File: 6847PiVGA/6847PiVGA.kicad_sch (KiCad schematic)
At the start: 38 parts, among them J1 DB15_Female_HighDensity, U1 MC6847, U2 AD724JRZ, U3 Pico, U4 AD813, Y1 4.433620MHz

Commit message: refine hardware layout
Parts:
- J1: footprint Resistor_SMD:R_0603_1608Metric -> Connector_Dsub:DSUB-15-HD_Female_Horizontal_P2.29x1.98mm_EdgePinOffset3.03mm_Housed_MountingHolesOffset4.94mm
- U3: footprint RPi_Pico:RPi_Pico_SMD_TH -> Package_DIP:DIP-42_W15.24mm
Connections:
- net at R12.1, R7.1, R8.1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: now also C1.2, J1.3; no longer C3.2, J1.1
- net at R1.1, R10.1, R2.1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: now also C3.2, J1.1; no longer C1.2, J1.3
- no-connect marks 19 -> 31

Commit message: board refresh
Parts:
- C1, C10, C2, C3, C4, C5, C6, C7, C8, C9: footprint Capacitor_SMD:C_0603_1608Metric -> Capacitor_SMD:C_0805_2012Metric
- R1, R10, R11, R12, R13, R14, R15, R16, R17, R18, R19, R20, R21, R22, R5, R8: footprint Resistor_SMD:R_0603_1608Metric -> Resistor_SMD:R_0805_2012Metric
- R2: value 1K -> 2K; footprint Resistor_SMD:R_0603_1608Metric -> Resistor_SMD:R_0805_2012Metric
- R3, R6, R9: value 2K -> 499R; footprint Resistor_SMD:R_0603_1608Metric -> Resistor_SMD:R_0805_2012Metric
- R4, R7: value 499R -> 2K; footprint Resistor_SMD:R_0603_1608Metric -> Resistor_SMD:R_0805_2012Metric
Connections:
- net +5V: now also U3.39 (VSYS); no longer U3.40 (VBUS)
- net GND: now also J1.10, J1.5, J1.7, U3.18 (GND), U3.23 (GND), U3.28 (GND), U3.3 (GND), U3.33 (AGND), U3.8 (GND)
- net Vsync: now reaches U1.12 (~{MS}), U1.37 (~{FS}), U2.15 (VSYNC), U3.17 (GPIO13)
- net Vsync: now also J1.14; no longer J1.13
- net DD6: now reaches U1.2 (DD6), U1.32 (INV), U3.9 (GPIO6)
- net Atiming: now reaches U1.22 (DA0), U3.20 (GPIO15)
- net GM2: now reaches U1.27 (GM2), U3.14 (GPIO10)
- net GM1: now reaches U1.29 (GM1), U3.12 (GPIO9)
- net DD0: now reaches U1.3 (DD0), U3.1 (GPIO0)
- net GM0: now reaches U1.30 (GM0), U1.31 (~{INT}/EXT), U3.11 (GPIO8)
- net CLK: now reaches U1.33 (CLK), U3.16 (GPIO12)
- net DD7: now reaches U1.34 (~{A}/S), U1.40 (DD7), U3.10 (GPIO7)
- net ~{A}/G: now reaches U1.35 (~{A}/G), U3.19 (GPIO14)
- net Hsync: now reaches U1.38 (~{HS}), U2.16 (HSYNC), U3.21 (GPIO16)
- net Hsync: now also J1.13; no longer J1.14
- net CSS: now reaches U1.39 (CSS), U3.15 (GPIO11)
- net DD1: now reaches U1.4 (DD1), U3.2 (GPIO1)
- net DD2: now reaches U1.5 (DD2), U3.4 (GPIO2)
- net DD3: now reaches U1.6 (DD3), U3.5 (GPIO3)
- net DD4: now reaches U1.7 (DD4), U3.6 (GPIO4)
- net DD5: now reaches U1.8 (DD5), U3.7 (GPIO5)
- net Gvga: now reaches C2.2, J1.2, R11.1, R4.1, R5.1, R6.1, U4.12 (+)
- net at R6.2: now also U3.29 (GPIO22); no longer U3.26 (GPIO20)
- net Bvga: now reaches C1.2, J1.3, R12.1, R7.1, R8.1, R9.1, U4.10 (+)
- net at R7.2: now also U3.22 (GPIO17); no longer U3.25 (GPIO19)
- net Composite: now reaches C9.1, U2.10 (COMP)
- net Rin: now reaches C3.1, U2.6 (RIN)
- net Gin: now reaches C2.1, U2.7 (GIN)
- net Bin: now reaches C1.1, U2.8 (BIN)
- net Rvga: now reaches C3.2, J1.1, R1.1, R10.1, R2.1, R3.1, U4.5 (+)
- net at R3.2: now also U3.34 (GPIO28_ADC2); no longer U3.31 (GPIO26_ADC0)
- net at R9.2: now also U3.25 (GPIO19); no longer U3.22 (GPIO17)
- net at R4.2: now also U3.26 (GPIO20); no longer U3.29 (GPIO22)
- net at R1.2: now also U3.31 (GPIO26_ADC0); no longer U3.34 (GPIO28_ADC2)
- no-connect marks 31 -> 28
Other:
- moved on the sheet: C1, C10, C2, C3, C4, C5, C6, C7, C8, C9, J1, R1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

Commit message: add power protection
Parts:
- added C11: 10uF, Capacitor_SMD:C_0805_2012Metric, symbol Device:C
- added D1: 1N5817, Diode_SMD:D_SOD-523, symbol Diode:1N5817
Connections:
- net +5V: now also C11.1, D1.2 (A); no longer U3.39 (VSYS)
- net GND: now also C11.2
- new net: D1.1 (K), U3.39 (VSYS)
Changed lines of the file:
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@@
     (comment 2 "Provides VGA, RGB and Composite video output")
   )
+  (junction (at 142.875 48.895) (diameter 0) (color 0 0 0 0)
+  )
   (junction (at 42.164 23.749) (diameter 0) (color 0 0 0 0)
   )
@@
   )
   (junction (at 262.763 24.511) (diameter 0) (color 0 0 0 0)
+  )
+  (junction (at 142.875 56.515) (diameter 0) (color 0 0 0 0)
   )
   (junction (at 237.363 49.911) (diameter 0) (color 0 0 0 0)
@@
     (stroke (width 0) (type default) (color 0 0 0 0))
   )
+  (wire (pts (xy 136.525 48.895) (xy 142.875 48.895))
+    (stroke (width 0) (type default) (color 0 0 0 0))
+  )
   (wire (pts (xy 127 74.295) (xy 125.73 74.295))
     (stroke (width 0) (type default) (color 0 0 0 0))
@@
     (stroke (width 0) (type default) (color 0 0 0 0))
   )
+  (wire (pts (xy 142.875 56.515) (xy 125.73 56.515))
+    (stroke (width 0) (type default) (color 0 0 0 0))
+  )
   (wire (pts (xy 40.005 145.923) (xy 28.448 145.923))
     (stroke (width 0) (type default) (color 0 0 0 0))
@@
     (stroke (width 0) (type default) (color 0 0 0 0))
   )
+  (wire (pts (xy 136.525 53.975) (xy 136.525 48.895))
+    (stroke (width 0) (type default) (color 0 0 0 0))
+  )
   (wire (pts (xy 29.718 138.303) (xy 31.115 138.303))
     (stroke (width 0) (type default) (color 0 0 0 0))
@@
   )
   (wire (pts (xy 42.164 23.749) (xy 42.164 25.527))
+    (stroke (width 0) (type default) (color 0 0 0 0))
+  )
+  (wire (pts (xy 128.905 53.975) (xy 125.73 53.975))
     (stroke (width 0) (type default) (color 0 0 0 0))
   )
@@
       (effects (font (size 1.27 1.27)) hide)
     )
+    (pin "1")
+    (pin "5")
+    (pin "6")
+    (pin "7")
+    (pin "12")
+    (pin "13")
+    (pin "14")
+    (pin "2")
     (pin "10")
     (pin "3")
     (pin "8")
     (pin "9")
+    (pin "11")
+    (pin "4")
   )
   (symbol (lib_id "power:GND") (at 90.17 94.615 270) (unit 1)
@@
     (pin "1")
   )
+  (symbol (lib_id "power:+5V") (at 142.875 48.895 270) (unit 1)
+    (in_bom yes) (on_board yes) (fields_autoplaced)
+    (property "Reference" "#PWR02" (id 0) (at 139.065 48.895 0)
+      (effects (font (size 1.27 1.27)) hide)
+    )
+    (property "Value" "+5V" (id 1) (at 146.685 48.8949 90)
+      (effects (font (size 1.27 1.27)) (justify left))
+    )
+    (property "Footprint" "" (id 2) (at 142.875 48.895 0)
+      (effects (font (size 1.27 1.27)) hide)
+    )
+    (property "Datasheet" "" (id 3) (at 142.875 48.895 0)
+      (effects (font (size 1.27 1.27)) hide)
+    )
+    (pin "1")
+  )
   (symbol (lib_id "power:GND") (at 125.73 69.215 90) (unit 1)
     (in_bom yes) (on_board yes) (fields_autoplaced)
@@
     )
     (pin "1")
+  )
+  (symbol (lib_id "Diode:1N5817") (at 132.715 53.975 0) (unit 1)
+    (in_bom yes) (on_board yes) (fields_autoplaced)
+    (property "Reference" "D1" (id 0) (at 132.3975 47.625 0))
+    (property "Value" "1N5817" (id 1) (at 132.3975 50.165 0))
+    (property "Footprint" "Diode_SMD:D_SOD-523" (id 2) (at 132.715 58.42 0)
+      (effects (font (size 1.27 1.27)) hide)
+    )
+    (property "Datasheet" "http://www.vishay.com/docs/88525/1n5817.pdf" (id 3) (at 132.715 53.975 0)
+      (effects (font (size 1.27 1.27)) hide)
+    )
+    (pin "1")
+    (pin "2")
   )
   (symbol (lib_id "Device:R") (at 130.81 84.455 270) (unit 1)
@@
       (effects (font (size 1.27 1.27)) hide)
     )
+    (pin "1")
+    (pin "5")
+    (pin "6")
+    (pin "7")
+    (pin "12")
+    (pin "13")
+    (pin "14")
+    (pin "2")
+    (pin "10")
+    (pin "3")
+    (pin "8")
+    (pin "9")
     (pin "11")
     (pin "4")
@@
     (pin "2")
   )
-  (symbol (lib_id "power:GND") (at 125.73 56.515 90) (unit 1)
-    (in_bom yes) (on_board yes) (fields_autoplaced)
-    (property "Reference" "#PWR0115" (id 0) (at 132.08 56.515 0)
-      (effects (font (size 1.27 1.27)) hide)
-    )
-    (property "Value" "GND" (id 1) (at 129.54 56.5149 90)
-      (effects (font (size 1.27 1.27)) (justify right) hide)
-    )
-    (property "Footprint" "" (id 2) (at 125.73 56.515 0)
-      (effects (font (size 1.27 1.27)) hide)
-    )
-    (property "Datasheet" "" (id 3) (at 125.73 56.515 0)
+  (symbol (lib_id "power:GND") (at 142.875 56.515 90) (unit 1)
+    (in_bom yes) (on_board yes) (fields_autoplaced)
+    (property "Reference" "#PWR0115" (id 0) (at 149.225 56.515 0)
+      (effects (font (size 1.27 1.27)) hide)
+    )
+    (property "Value" "GND" (id 1) (at 146.685 56.5149 90)
+      (effects (font (size 1.27 1.27)) (justify right) hide)
+    )
+    (property "Footprint" "" (id 2) (at 142.875 56.515 0)
+      (effects (font (size 1.27 1.27)) hide)
+    )
+    (property "Datasheet" "" (id 3) (at 142.875 56.515 0)
       (effects (font (size 1.27 1.27)) hide)
     )
@@
     (pin "1")
   )
+  (symbol (lib_id "Device:C") (at 142.875 52.705 0) (unit 1)
+    (in_bom yes) (on_board yes) (fields_autoplaced)
+    (property "Reference" "C11" (id 0) (at 146.685 51.4349 0)
+      (effects (font (size 1.27 1.27)) (justify left))
+    )
+    (property "Value" "10uF" (id 1) (at 146.685 53.9749 0)
+      (effects (font (size 1.27 1.27)) (justify left))
+    )
+    (property "Footprint" "Capacitor_SMD:C_0805_2012Metric" (id 2) (at 143.8402 56.515 0)
+      (effects (font (size 1.27 1.27)) hide)
+    )
+    (property "Datasheet" "~" (id 3) (at 142.875 52.705 0)
+      (effects (font (size 1.27 1.27)) hide)
+    )
+    (pin "1")
+    (pin "2")
+  )
   (symbol (lib_id "Device:R") (at 256.413 49.911 90) (unit 1)
     (in_bom yes) (on_board yes) (fields_autoplaced)
@@
       (effects (font (size 1.27 1.27)) hide)
     )
+    (pin "1")
+    (pin "5")
+    (pin "6")
+    (pin "7")
     (pin "12")
     (pin "13")
     (pin "14")
     (pin "2")
-  )
-  (symbol (lib_id "power:+5V") (at 125.73 53.975 270) (unit 1)
-    (in_bom yes) (on_board yes) (fields_autoplaced)
-    (property "Reference" "#PWR02" (id 0) (at 121.92 53.975 0)
-      (effects (font (size 1.27 1.27)) hide)
-    )
-    (property "Value" "+5V" (id 1) (at 129.54 53.9749 90)
-      (effects (font (size 1.27 1.27)) (justify left))
-    )
-    (property "Footprint" "" (id 2) (at 125.73 53.975 0)
-      (effects (font (size 1.27 1.27)) hide)
-    )
-    (property "Datasheet" "" (id 3) (at 125.73 53.975 0)
-      (effects (font (size 1.27 1.27)) hide)
-    )
-    (pin "1")
+    (pin "10")
+    (pin "3")
+    (pin "8")
+    (pin "9")
+    (pin "11")
+    (pin "4")
   )
   (symbol (lib_id "power:GND") (at 210.185 85.725 0) (unit 1)
@@
     (pin "6")
     (pin "7")
+    (pin "12")
+    (pin "13")
+    (pin "14")
+    (pin "2")
+    (pin "10")
+    (pin "3")
+    (pin "8")
+    (pin "9")
+    (pin "11")
+    (pin "4")
   )
   (symbol (lib_id "Device:C") (at 208.28 99.695 0) (unit 1)
@@
       (reference "#PWR01") (unit 1) (value "GND") (footprint "")
     )
-    (path "/7a749901-be0b-4432-aaf8-b59971568121"
+    (path "/26cb9b96-c0cb-40c8-90fa-6343f70293fe"
       (reference "#PWR02") (unit 1) (value "+5V") (footprint "")
     )
@@
       (reference "C10") (unit 1) (value "0.1uF") (footprint "Capacitor_SMD:C_0805_2012Metric")
     )
+    (path "/70beb333-84c4-4efc-9f6a-99dcba956560"
+      (reference "C11") (unit 1) (value "10uF") (footprint "Capacitor_SMD:C_0805_2012Metric")
+    )
+    (path "/2c8b1290-7502-48d0-b143-1873563d1c89"
+      (reference "D1") (unit 1) (value "1N5817") (footprint "Diode_SMD:D_SOD-523")
+    )
     (path "/f41990df-ad91-4392-9d26-43396dd7ca37"

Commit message: correct pico footprint
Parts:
- added J2: Conn_01x06_Male, Connector_PinHeader_2.54mm:PinHeader_1x06_P2.54mm_Vertical, symbol Connector:Conn_01x06_Male
- U3: footprint Package_DIP:DIP-42_W15.24mm -> Package_DIP:DIP-40_W15.24mm
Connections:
- net +5V: no longer C10.1, C4.1, C5.2, C6.1, C7.2, U2.14 (DPOS), U2.4 (APOS), U2.5 (ENCD), U4.4 (V+)
- net B: now also J2.1 (Pin_1)
- net Comp: now also J2.6 (Pin_6)
- net G: now also J2.2 (Pin_2)
- net GND: now also J2.4 (Pin_4), J2.5 (Pin_5)
- net R: now also J2.3 (Pin_3)
- net +5VD: now reaches D1.1 (K), U3.39 (VSYS)
- net +5VD: now also C10.1, C4.1, C5.2, C6.1, C7.2, U2.14 (DPOS), U2.4 (APOS), U2.5 (ENCD), U4.4 (V+)

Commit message: .
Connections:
- net CLK renamed VCLK
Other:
- moved on the sheet: J1

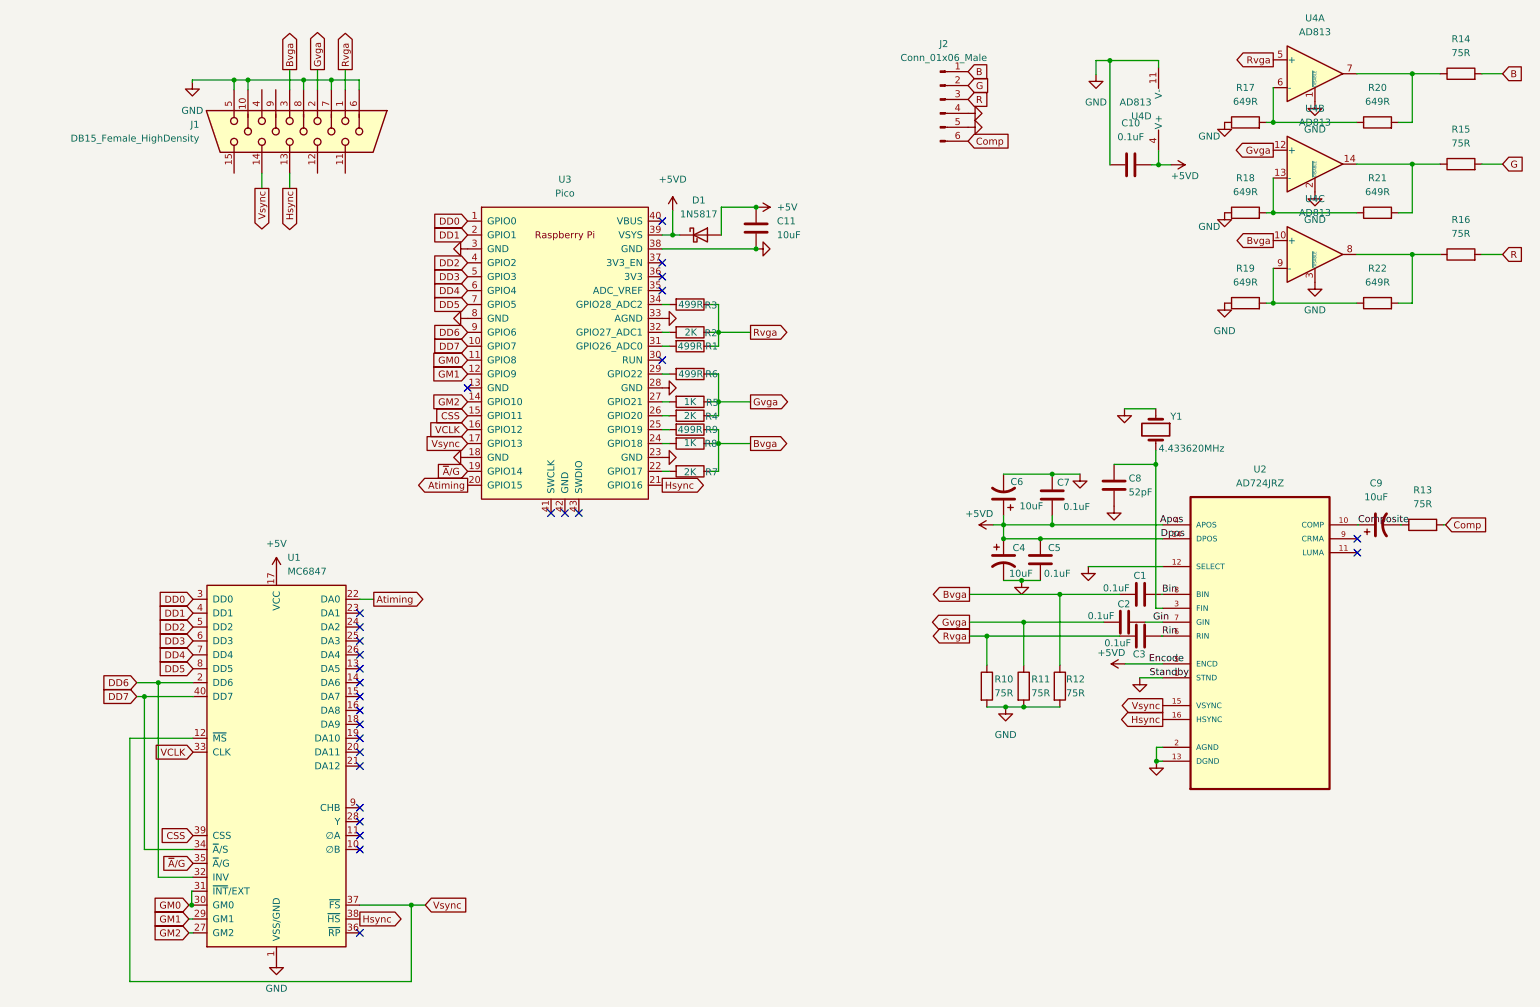
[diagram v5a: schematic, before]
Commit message: add level shift
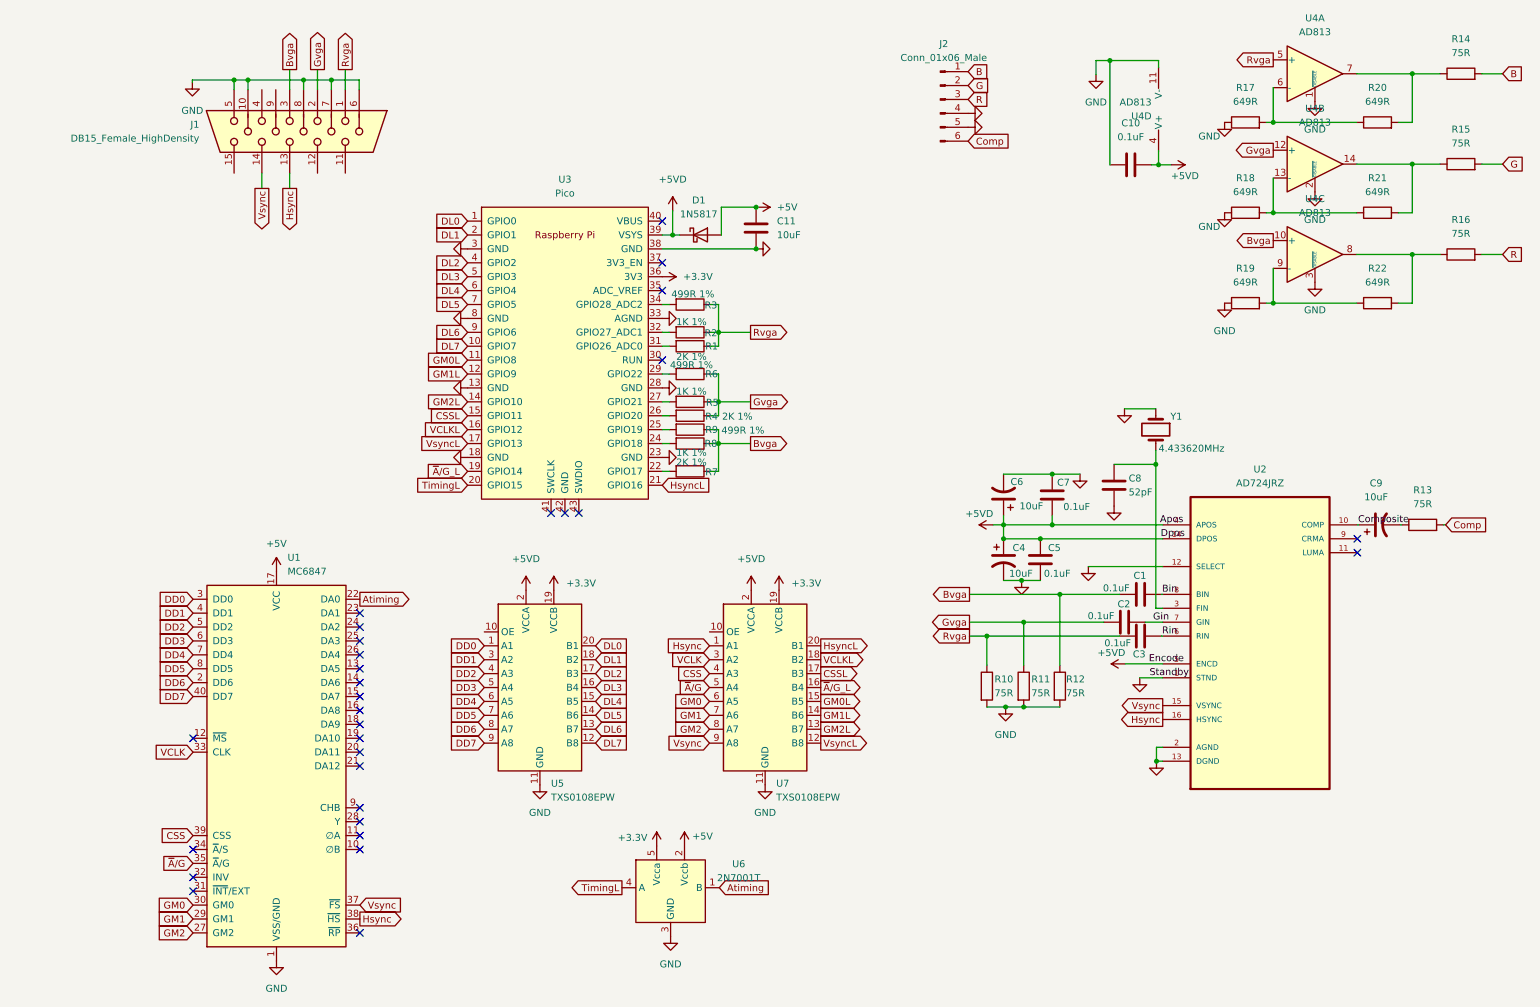
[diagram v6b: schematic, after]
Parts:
- added U5, U7: TXS0108EPW, Package_SO:TSSOP-20_4.4x6.5mm_P0.65mm, symbol Logic_LevelTranslator:TXS0108EPW
- added U6: 2N7001T, Package_TO_SOT_SMD:SOT-353_SC-70-5, symbol 6847P:2N7001T
- R1: value 499R -> 2K 1%
- R2: value 2K -> 1K 1%
- R3, R6, R9: value 499R -> 499R 1%
- R4, R7: value 2K -> 2K 1%
- R5, R8: value 1K -> 1K 1%
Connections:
- net +5V: now also U6.2 (Vccb)
- net +5VD: now also U5.2 (VCCA), U7.2 (VCCA)
- net Atiming: now also U6.1 (B); no longer U3.20 (GPIO15)
- net CSS: now also U7.4 (A3); no longer U3.15 (GPIO11)
- net DD0: now also U5.1 (A1); no longer U3.1 (GPIO0)
- net DD1: now also U5.3 (A2); no longer U3.2 (GPIO1)
- net DD2: now also U5.4 (A3); no longer U3.4 (GPIO2)
- net DD3: now also U5.5 (A4); no longer U3.5 (GPIO3)
- net DD4: now also U5.6 (A5); no longer U3.6 (GPIO4)
- net DD5: now also U5.7 (A6); no longer U3.7 (GPIO5)
- net DD6: now also U5.8 (A7); no longer U1.32 (INV), U3.9 (GPIO6)
- net DD7: now also U5.9 (A8); no longer U1.34 (~{A}/S), U3.10 (GPIO7)
- net GM0: now also U7.6 (A5); no longer U1.31 (~{INT}/EXT), U3.11 (GPIO8)
- net GM1: now also U7.7 (A6); no longer U3.12 (GPIO9)
- net GM2: now also U7.8 (A7); no longer U3.14 (GPIO10)
- net GND: now also U3.13 (GND), U5.11 (GND), U6.3 (GND), U7.11 (GND)
- net Hsync: now also U7.1 (A1); no longer U3.21 (GPIO16)
- net VCLK: now also U7.3 (A2); no longer U3.16 (GPIO12)
- net Vsync: now also U7.9 (A8); no longer U1.12 (~{MS}), U3.17 (GPIO13)
- net ~{A}/G: now also U7.5 (A4); no longer U3.19 (GPIO14)
- net +3.3V: now reaches U3.36 (3V3)
- net +3.3V: now also U5.19 (VCCB), U6.5 (Vcca), U7.19 (VCCB)
- new net CSSL: U3.15 (GPIO11), U7.17 (B3)
- new net DL0: U3.1 (GPIO0), U5.20 (B1)
- new net DL1: U3.2 (GPIO1), U5.18 (B2)
- new net DL2: U3.4 (GPIO2), U5.17 (B3)
- new net DL3: U3.5 (GPIO3), U5.16 (B4)
- new net DL4: U3.6 (GPIO4), U5.15 (B5)
- new net DL5: U3.7 (GPIO5), U5.14 (B6)
- new net DL6: U3.9 (GPIO6), U5.13 (B7)
- new net DL7: U3.10 (GPIO7), U5.12 (B8)
- new net GM0L: U3.11 (GPIO8), U7.15 (B5)
- new net GM1L: U3.12 (GPIO9), U7.14 (B6)
- new net GM2L: U3.14 (GPIO10), U7.13 (B7)
- new net HsyncL: U3.21 (GPIO16), U7.20 (B1)
- new net TimingL: U3.20 (GPIO15), U6.4 (A)
- new net VCLKL: U3.16 (GPIO12), U7.18 (B2)
- new net VsyncL: U3.17 (GPIO13), U7.12 (B8)
- new net ~{A}/G_L: U3.19 (GPIO14), U7.16 (B4)
- no-connect marks 28 -> 30
